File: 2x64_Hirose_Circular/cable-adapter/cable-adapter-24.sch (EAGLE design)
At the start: 48 parts

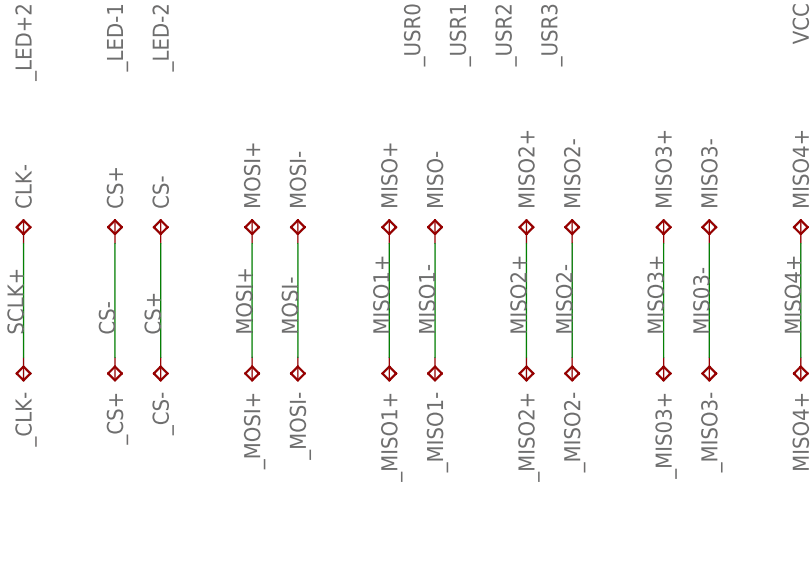
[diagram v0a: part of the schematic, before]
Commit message: Toward SPI interface board rev 1.2
- Added jumpers for AUX IN breadboard
- Started basic layout
- Changes in SPI cable pinout will need to be reflected in the
  commutator adapter board.
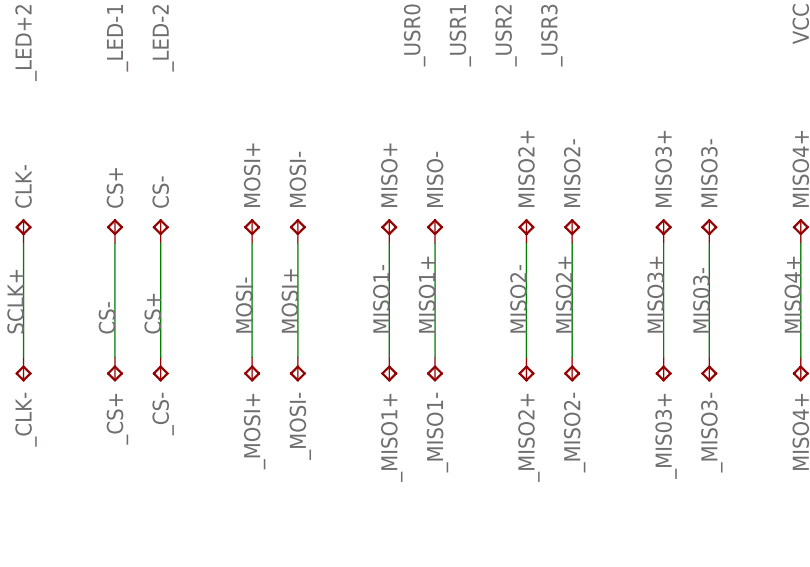
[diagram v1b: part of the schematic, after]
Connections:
- net MISO1+: now also MISO-.TP, _MISO1-.TP; no longer MISO+.TP, _MISO1+.TP
- net MISO1-: now also MISO+.TP, _MISO1+.TP; no longer MISO-.TP, _MISO1-.TP
- net MISO2+: now also MISO2-.TP, _MISO2-.TP; no longer MISO2+.TP, _MISO2+.TP
- net MISO2-: now also MISO2+.TP, _MISO2+.TP; no longer MISO2-.TP, _MISO2-.TP
- net MOSI+: now also MOSI-.TP, _MOSI-.TP; no longer MOSI+.TP, _MOSI+.TP
- net MOSI-: now also MOSI+.TP, _MOSI+.TP; no longer MOSI-.TP, _MOSI-.TP
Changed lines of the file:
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@@
-</segment>
-</net>
-<net name="MOSI+" class="0">
-<segment>
-<pinref part="MOSI+" gate="G$1" pin="TP"/>
-<pinref part="_MOSI+" gate="G$1" pin="TP"/>
-<wire x1="167.64" y1="129.54" x2="167.64" y2="116.84" width="0.1524" layer="91"/>
-<label x="167.64" y="119.38" size="1.778" layer="95" rot="R90"/>
 </segment>
 </net>
@@
 <wire x1="218.44" y1="129.54" x2="218.44" y2="116.84" width="0.1524" layer="91"/>
 <label x="218.44" y="119.38" size="1.778" layer="95" rot="R90"/>
-</segment>
-</net>
-<net name="MISO2+" class="0">
-<segment>
-<pinref part="MISO2+" gate="G$1" pin="TP"/>
-<pinref part="_MISO2+" gate="G$1" pin="TP"/>
-<wire x1="198.12" y1="129.54" x2="198.12" y2="116.84" width="0.1524" layer="91"/>
-<label x="198.12" y="119.38" size="1.778" layer="95" rot="R90"/>
 </segment>
 </net>
@@
 <net name="MOSI-" class="0">
 <segment>
-<pinref part="MOSI-" gate="G$1" pin="TP"/>
-<pinref part="_MOSI-" gate="G$1" pin="TP"/>
-<wire x1="172.72" y1="129.54" x2="172.72" y2="116.84" width="0.1524" layer="91"/>
-<label x="172.72" y="119.38" size="1.778" layer="95" rot="R90"/>
+<pinref part="MOSI+" gate="G$1" pin="TP"/>
+<pinref part="_MOSI+" gate="G$1" pin="TP"/>
+<wire x1="167.64" y1="129.54" x2="167.64" y2="116.84" width="0.1524" layer="91"/>
+<label x="167.64" y="119.38" size="1.778" layer="95" rot="R90"/>
 </segment>
 </net>
 <net name="MISO1-" class="0">
-<segment>
-<pinref part="MISO-" gate="G$1" pin="TP"/>
-<pinref part="_MISO1-" gate="G$1" pin="TP"/>
-<wire x1="187.96" y1="129.54" x2="187.96" y2="116.84" width="0.1524" layer="91"/>
-<label x="187.96" y="119.38" size="1.778" layer="95" rot="R90"/>
-</segment>
-</net>
-<net name="MISO1+" class="0">
 <segment>
 <pinref part="MISO+" gate="G$1" pin="TP"/>
@@
 <net name="MISO2-" class="0">
 <segment>
-<pinref part="MISO2-" gate="G$1" pin="TP"/>
-<pinref part="_MISO2-" gate="G$1" pin="TP"/>
-<wire x1="203.2" y1="129.54" x2="203.2" y2="116.84" width="0.1524" layer="91"/>
-<label x="203.2" y="119.38" size="1.778" layer="95" rot="R90"/>
+<pinref part="MISO2+" gate="G$1" pin="TP"/>
+<pinref part="_MISO2+" gate="G$1" pin="TP"/>
+<wire x1="198.12" y1="129.54" x2="198.12" y2="116.84" width="0.1524" layer="91"/>
+<label x="198.12" y="119.38" size="1.778" layer="95" rot="R90"/>
 </segment>
 </net>
@@
 </segment>
 </net>
+<net name="MOSI+" class="0">
+<segment>
+<pinref part="MOSI-" gate="G$1" pin="TP"/>
+<pinref part="_MOSI-" gate="G$1" pin="TP"/>
+<wire x1="172.72" y1="129.54" x2="172.72" y2="116.84" width="0.1524" layer="91"/>
+<label x="172.72" y="119.38" size="1.778" layer="95" rot="R90"/>
+</segment>
+</net>
+<net name="MISO2+" class="0">
+<segment>
+<pinref part="MISO2-" gate="G$1" pin="TP"/>
+<pinref part="_MISO2-" gate="G$1" pin="TP"/>
+<wire x1="203.2" y1="129.54" x2="203.2" y2="116.84" width="0.1524" layer="91"/>
+<label x="203.2" y="119.38" size="1.778" layer="95" rot="R90"/>
+</segment>
+</net>
+<net name="MISO1+" class="0">
+<segment>
+<pinref part="MISO-" gate="G$1" pin="TP"/>
+<pinref part="_MISO1-" gate="G$1" pin="TP"/>
+<wire x1="187.96" y1="129.54" x2="187.96" y2="116.84" width="0.1524" layer="91"/>
+<label x="187.96" y="119.38" size="1.778" layer="95" rot="R90"/>
+</segment>
+</net>
